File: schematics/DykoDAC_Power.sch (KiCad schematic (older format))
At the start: 39 parts, among them J1 AC Input, U1 LT1762-5, U2 LM317, U3 LM337, U4 L7805, U5 78L05, U6 LP5907-3.3, U7 LP5907-3.3

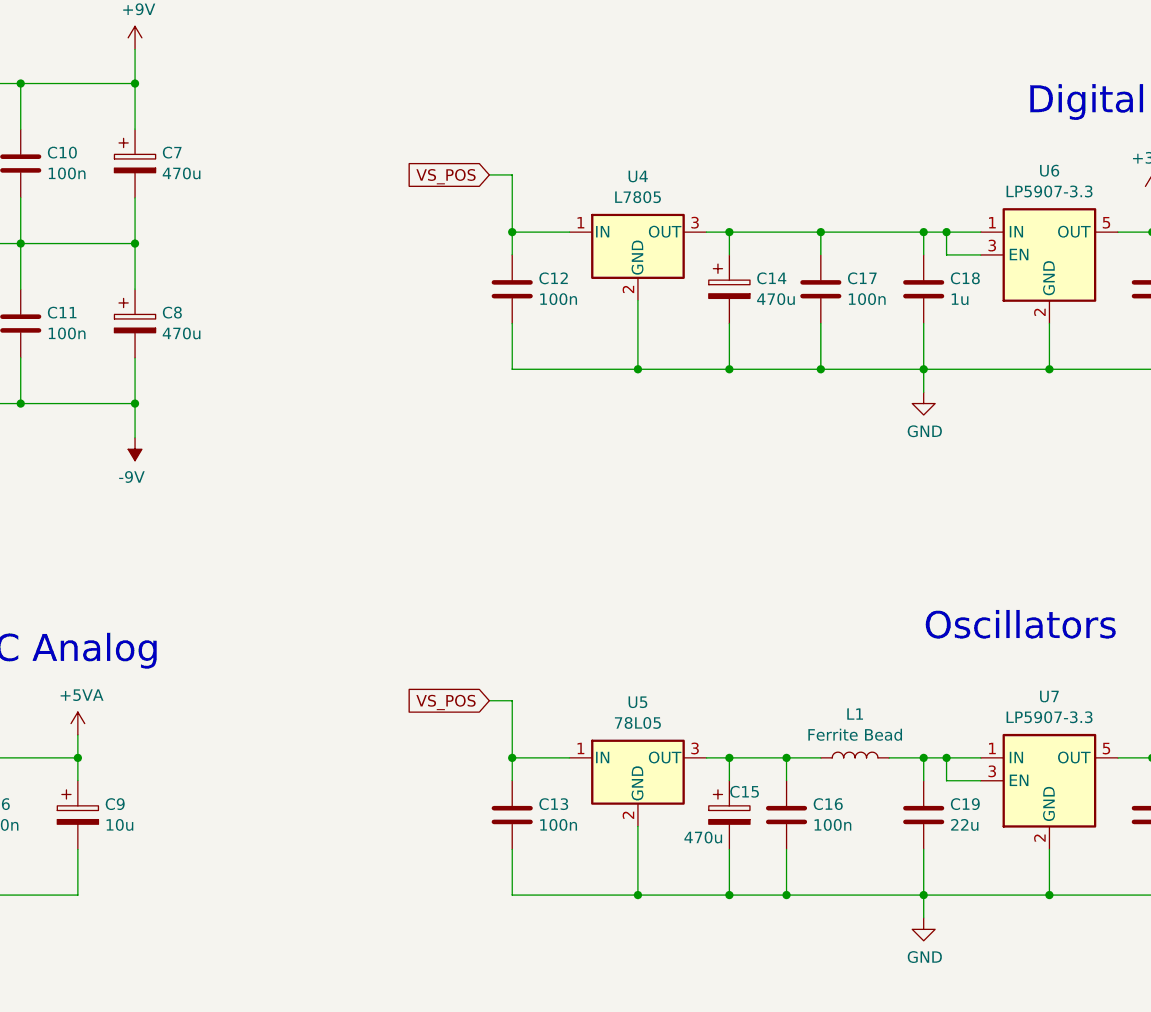
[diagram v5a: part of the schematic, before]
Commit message: opamp filter pcb
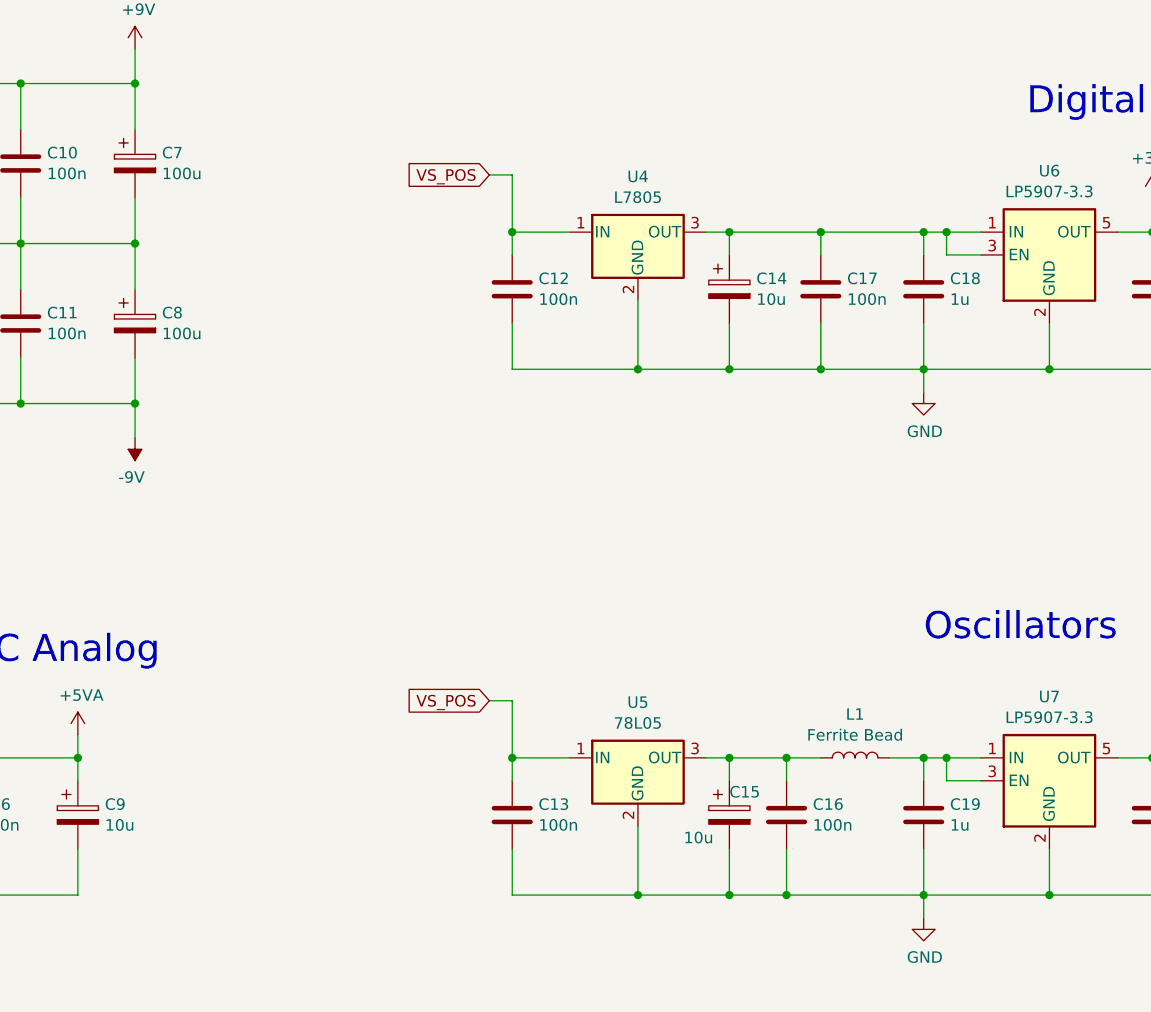
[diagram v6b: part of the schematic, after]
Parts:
- C13: footprint Capacitors_SMD:C_0603_HandSoldering -> Capacitors_SMD:C_0603
- C14, C15: value 470u -> 10u; footprint Capacitors_SMD:CP_Elec_8x6.7 -> Capacitors_Tantalum_SMD:CP_Tantalum_Case-A_EIA-3216-18_Reflow
- C19: value 22u -> 1u
- C64, C65: footprint (none) -> Capacitors_Tantalum_SMD:CP_Tantalum_Case-A_EIA-3216-18_Reflow
- C7: value 470u -> 100u; footprint Capacitors_SMD:CP_Elec_8x6.7 -> Capacitors_Tantalum_SMD:CP_Tantalum_Case-D_EIA-7343-31_Reflow; Part (none) -> TAJD107K016SNJ
- C8: value 470u -> 100u; footprint Capacitors_SMD:CP_Elec_8x6.7 -> Capacitors_Tantalum_SMD:CP_Tantalum_Case-D_EIA-7343-31_Reflow
- C9: footprint Capacitors_SMD:CP_Elec_4x5.7 -> Capacitors_Tantalum_SMD:CP_Tantalum_Case-A_EIA-3216-18_Reflow; Part (none) -> T491A106K016AT
- R40, R41, R42, R43: footprint (none) -> Resistors_SMD:R_0603
- U2, U3, U4: footprint TO_SOT_Packages_SMD:TO-263-2 -> TO_SOT_Packages_SMD:SOT-223-3_TabPin2
- U5: footprint TO_SOT_Packages_SMD:SOT-89-3 -> TO_SOT_Packages_SMD:SOT-23
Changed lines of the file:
@@
 P 4950 2500
 F 0 "C8" H 5068 2546 50  0000 L CNN
-F 1 "470u" H 5068 2455 50  0000 L CNN
-F 2 "Capacitors_SMD:CP_Elec_8x6.7" H 4988 2350 50  0001 C CNN
+F 1 "100u" H 5068 2455 50  0000 L CNN
+F 2 "Capacitors_Tantalum_SMD:CP_Tantalum_Case-D_EIA-7343-31_Reflow" H 4988 2350 50  0001 C CNN
 F 3 "~" H 4950 2500 50  0001 C CNN
 	1    4950 2500
@@
 P 4950 1800
 F 0 "C7" H 5068 1846 50  0000 L CNN
-F 1 "470u" H 5068 1755 50  0000 L CNN
-F 2 "Capacitors_SMD:CP_Elec_8x6.7" H 4988 1650 50  0001 C CNN
+F 1 "100u" H 5068 1755 50  0000 L CNN
+F 2 "Capacitors_Tantalum_SMD:CP_Tantalum_Case-D_EIA-7343-31_Reflow" H 4988 1650 50  0001 C CNN
 F 3 "~" H 4950 1800 50  0001 C CNN
+F 4 "TAJD107K016SNJ " H 4950 1800 50  0001 C CNN "Part"
 	1    4950 1800
 	1    0    0    -1
@@
 F 0 "C9" H 4818 4696 50  0000 L CNN
 F 1 "10u" H 4818 4605 50  0000 L CNN
-F 2 "Capacitors_SMD:CP_Elec_4x5.7" H 4738 4500 50  0001 C CNN
+F 2 "Capacitors_Tantalum_SMD:CP_Tantalum_Case-A_EIA-3216-18_Reflow" H 4738 4500 50  0001 C CNN
 F 3 "~" H 4700 4650 50  0001 C CNN
+F 4 "T491A106K016AT " H 4700 4650 50  0001 C CNN "Part"
 	1    4700 4650
 	1    0    0    -1
@@
 P 7550 2350
 F 0 "C14" H 7668 2396 50  0000 L CNN
-F 1 "470u" H 7668 2305 50  0000 L CNN
-F 2 "Capacitors_SMD:CP_Elec_8x6.7" H 7588 2200 50  0001 C CNN
+F 1 "10u" H 7668 2305 50  0000 L CNN
+F 2 "Capacitors_Tantalum_SMD:CP_Tantalum_Case-A_EIA-3216-18_Reflow" H 7588 2200 50  0001 C CNN
 F 3 "~" H 7550 2350 50  0001 C CNN
 	1    7550 2350
@@
 F 0 "U4" H 7150 2342 50  0000 C CNN
 F 1 "L7805" H 7150 2251 50  0000 C CNN
-F 2 "TO_SOT_Packages_SMD:TO-263-2" H 7175 1950 50  0001 L CIN
+F 2 "TO_SOT_Packages_SMD:SOT-223-3_TabPin2" H 7175 1950 50  0001 L CIN
 F 3 "http://www.st.com/content/ccc/resource/technical/document/datasheet/41/4f/b3/b0/12/d4/47/88/CD00000444.pdf/files/CD00000444.pdf/jcr:content/translations/en.CD00000444.pdf" H 7150 2050 50  0001 C CNN
 	1    7150 2100
@@
 P 8400 4650
 F 0 "C19" H 8515 4696 50  0000 L CNN
-F 1 "22u" H 8515 4605 50  0000 L CNN
+F 1 "1u" H 8515 4605 50  0000 L CNN
 F 2 "Capacitors_SMD:C_0603" H 8438 4500 50  0001 C CNN
 F 3 "~" H 8400 4650 50  0001 C CNN
@@
 P 7550 4650
 F 0 "C15" H 7550 4750 50  0000 L CNN
-F 1 "470u" H 7350 4550 50  0000 L CNN
-F 2 "Capacitors_SMD:CP_Elec_8x6.7" H 7588 4500 50  0001 C CNN
+F 1 "10u" H 7350 4550 50  0000 L CNN
+F 2 "Capacitors_Tantalum_SMD:CP_Tantalum_Case-A_EIA-3216-18_Reflow" H 7588 4500 50  0001 C CNN
 F 3 "~" H 7550 4650 50  0001 C CNN
 	1    7550 4650
@@
 F 0 "C13" H 6715 4696 50  0000 L CNN
 F 1 "100n" H 6715 4605 50  0000 L CNN
-F 2 "Capacitors_SMD:C_0603_HandSoldering" H 6638 4500 50  0001 C CNN
+F 2 "Capacitors_SMD:C_0603" H 6638 4500 50  0001 C CNN
 F 3 "~" H 6600 4650 50  0001 C CNN
 	1    6600 4650
@@
 F 0 "U5" H 7150 4642 50  0000 C CNN
 F 1 "78L05" H 7150 4551 50  0000 C CNN
-F 2 "TO_SOT_Packages_SMD:SOT-89-3" H 7175 4250 50  0001 L CIN
+F 2 "TO_SOT_Packages_SMD:SOT-23" H 7175 4250 50  0001 L CIN
 F 3 "http://www.st.com/content/ccc/resource/technical/document/datasheet/41/4f/b3/b0/12/d4/47/88/CD00000444.pdf/files/CD00000444.pdf/jcr:content/translations/en.CD00000444.pdf" H 7150 4350 50  0001 C CNN
 	1    7150 4400
@@
 F 0 "U3" H 3700 2701 50  0000 C CNN
 F 1 "LM337" H 3700 2610 50  0000 C CNN
-F 2 "TO_SOT_Packages_SMD:TO-263-2" H 3700 2650 50  0001 C CIN
+F 2 "TO_SOT_Packages_SMD:SOT-223-3_TabPin2" H 3700 2650 50  0001 C CIN
 F 3 "http://www.ti.com/lit/ds/symlink/lm337-n.pdf" H 3700 2850 50  0001 C CNN
 	1    3700 2850
@@
 F 0 "U2" H 3700 1208 50  0000 C CNN
 F 1 "LM317" H 3700 1299 50  0000 C CNN
-F 2 "TO_SOT_Packages_SMD:TO-263-2" H 3700 1250 50  0001 C CIN
+F 2 "TO_SOT_Packages_SMD:SOT-223-3_TabPin2" H 3700 1250 50  0001 C CIN
 F 3 "http://www.ti.com/lit/ds/symlink/lm337-n.pdf" H 3700 1450 50  0001 C CNN
 	1    3700 1450
@@
 F 0 "R41" H 4159 1996 50  0000 L CNN
 F 1 "1k5" H 4159 1905 50  0000 L CNN
-F 2 "" H 4100 1950 50  0001 C CNN
+F 2 "Resistors_SMD:R_0603" H 4100 1950 50  0001 C CNN
 F 3 "~" H 4100 1950 50  0001 C CNN
 	1    4100 1950
@@
 F 0 "R40" H 4159 1696 50  0000 L CNN
 F 1 "240" H 4159 1605 50  0000 L CNN
-F 2 "" H 4100 1650 50  0001 C CNN
+F 2 "Resistors_SMD:R_0603" H 4100 1650 50  0001 C CNN
 F 3 "~" H 4100 1650 50  0001 C CNN
 	1    4100 1650
@@
 F 0 "C64" H 3788 1996 50  0000 L CNN
 F 1 "10u" H 3800 1900 50  0000 L CNN
-F 2 "" H 3700 1950 50  0001 C CNN
+F 2 "Capacitors_Tantalum_SMD:CP_Tantalum_Case-A_EIA-3216-18_Reflow" H 3700 1950 50  0001 C CNN
 F 3 "~" H 3700 1950 50  0001 C CNN
 	1    3700 1950
@@
 F 0 "C65" H 3788 2396 50  0000 L CNN
 F 1 "10u" H 3800 2300 50  0000 L CNN
-F 2 "" H 3700 2350 50  0001 C CNN
+F 2 "Capacitors_Tantalum_SMD:CP_Tantalum_Case-A_EIA-3216-18_Reflow" H 3700 2350 50  0001 C CNN
 F 3 "~" H 3700 2350 50  0001 C CNN
 	1    3700 2350
@@
 F 0 "R43" H 4159 2696 50  0000 L CNN
 F 1 "240" H 4159 2605 50  0000 L CNN
-F 2 "" H 4100 2650 50  0001 C CNN
+F 2 "Resistors_SMD:R_0603" H 4100 2650 50  0001 C CNN
 F 3 "~" H 4100 2650 50  0001 C CNN
 	1    4100 2650
@@
 F 0 "R42" H 4159 2396 50  0000 L CNN
 F 1 "1k5" H 4159 2305 50  0000 L CNN
-F 2 "" H 4100 2350 50  0001 C CNN
+F 2 "Resistors_SMD:R_0603" H 4100 2350 50  0001 C CNN
 F 3 "~" H 4100 2350 50  0001 C CNN
 	1    4100 2350

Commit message: pcb
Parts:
- added C49: 100u, Capacitors_Tantalum_SMD:CP_Tantalum_Case-D_EIA-7343-31_Reflow, symbol Device:CP
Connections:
- net +3V3: now also C49.1
- net GND: now also C49.2
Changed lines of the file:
@@
 Wire Wire Line
 	4950 2850 4950 3000
+$Comp
+L Device:CP C49
+U 1 1 5EAF933C
+P 9850 2350
+F 0 "C49" H 9968 2396 50  0000 L CNN
+F 1 "100u" H 9968 2305 50  0000 L CNN
+F 2 "Capacitors_Tantalum_SMD:CP_Tantalum_Case-D_EIA-7343-31_Reflow" H 9888 2200 50  0001 C CNN
+F 3 "~" H 9850 2350 50  0001 C CNN
+	1    9850 2350
+	1    0    0    -1
+$EndComp
+Wire Wire Line
+	9400 2100 9850 2100
+Wire Wire Line
+	9850 2100 9850 2200
+Wire Wire Line
+	9850 2500 9850 2700
+Wire Wire Line
+	9850 2700 9400 2700
+Connection ~ 9400 2700
 $EndSCHEMATC

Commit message: pcb
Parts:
- J1: footprint Connect:BARREL_JACK -> Terminal_Blocks:TerminalBlock_Altech_AK300-2_P5.00mm
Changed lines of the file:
@@
 F 0 "J1" H 1070 2467 50  0000 C CNN
 F 1 "AC Input" H 1070 2376 50  0000 C CNN
-F 2 "Connect:BARREL_JACK" H 1150 2250 50  0001 C CNN
+F 2 "Terminal_Blocks:TerminalBlock_Altech_AK300-2_P5.00mm" H 1150 2250 50  0001 C CNN
 F 3 "~" H 1150 2250 50  0001 C CNN
 	1    1150 2250
